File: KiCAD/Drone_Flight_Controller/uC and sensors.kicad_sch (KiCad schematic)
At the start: 7 parts, among them U401 ESP32-WROOM-32, U402 DPS368, U403 BNO055

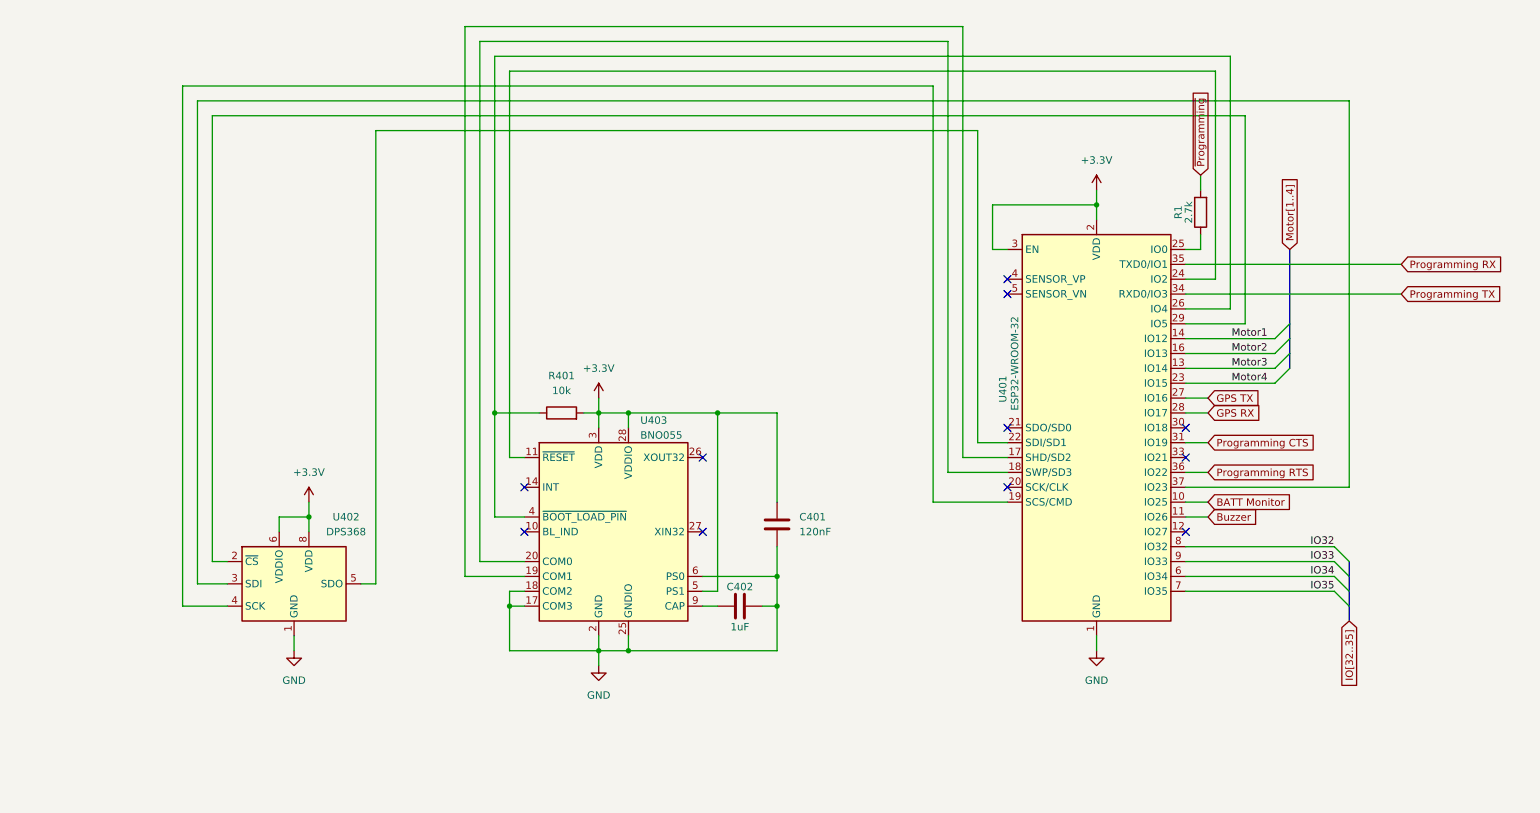
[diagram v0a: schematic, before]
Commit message: Fix SPI Connection, Disconnect wrong UART connection
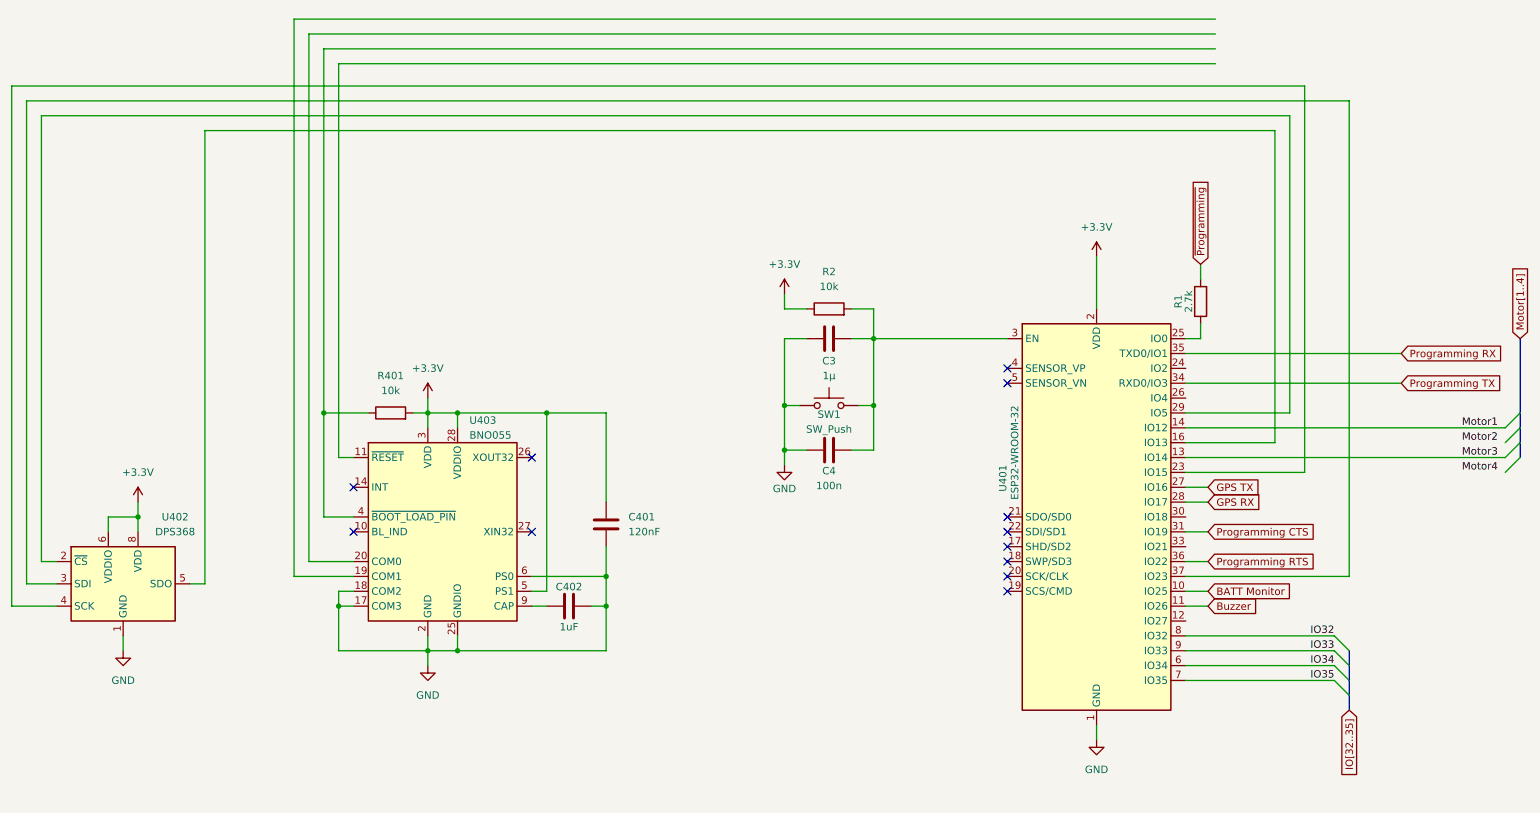
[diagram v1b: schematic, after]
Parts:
- added C3: 1µ, symbol Device:C
- added C4: 100n, Capacitor_SMD:C_0805_2012Metric_Pad1.18x1.45mm_HandSolder, symbol Device:C
- added R2: 10k, symbol Device:R
- added SW1: SW_Push, symbol Switch:SW_Push
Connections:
- net +3.3V: now also R2.1; no longer U401.3 (EN)
- net GND: now also C3.1, C4.1, SW1.1
- net Motor2: no longer U401.16 (IO13)
- net Motor4: no longer U401.23 (IO15)
- net at U401.17 (SHD/SD2): no longer U403.19 (COM1)
- net at U401.18 (SWP/SD3): no longer U403.20 (COM0)
- net at U401.19 (SCS/CMD): no longer U402.4 (SCK)
- net at U402.5 (SDO): now also U401.16 (IO13); no longer U401.22 (SDI/SD1)
- net at U401.24 (IO2): no longer U403.11 (~{RESET})
- net at R401.1, U403.4 (~{BOOT_LOAD_PIN}): no longer U401.26 (IO4)
- new net: U401.23 (IO15), U402.4 (SCK)
- new net: C3.2, C4.2, R2.2, SW1.2, U401.3 (EN)
- no-connect marks 11 -> 12
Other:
- moved on the sheet: C401, C402, R1, R401, U401, U402, U403

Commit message: Connect IMU via UART by IOMUX
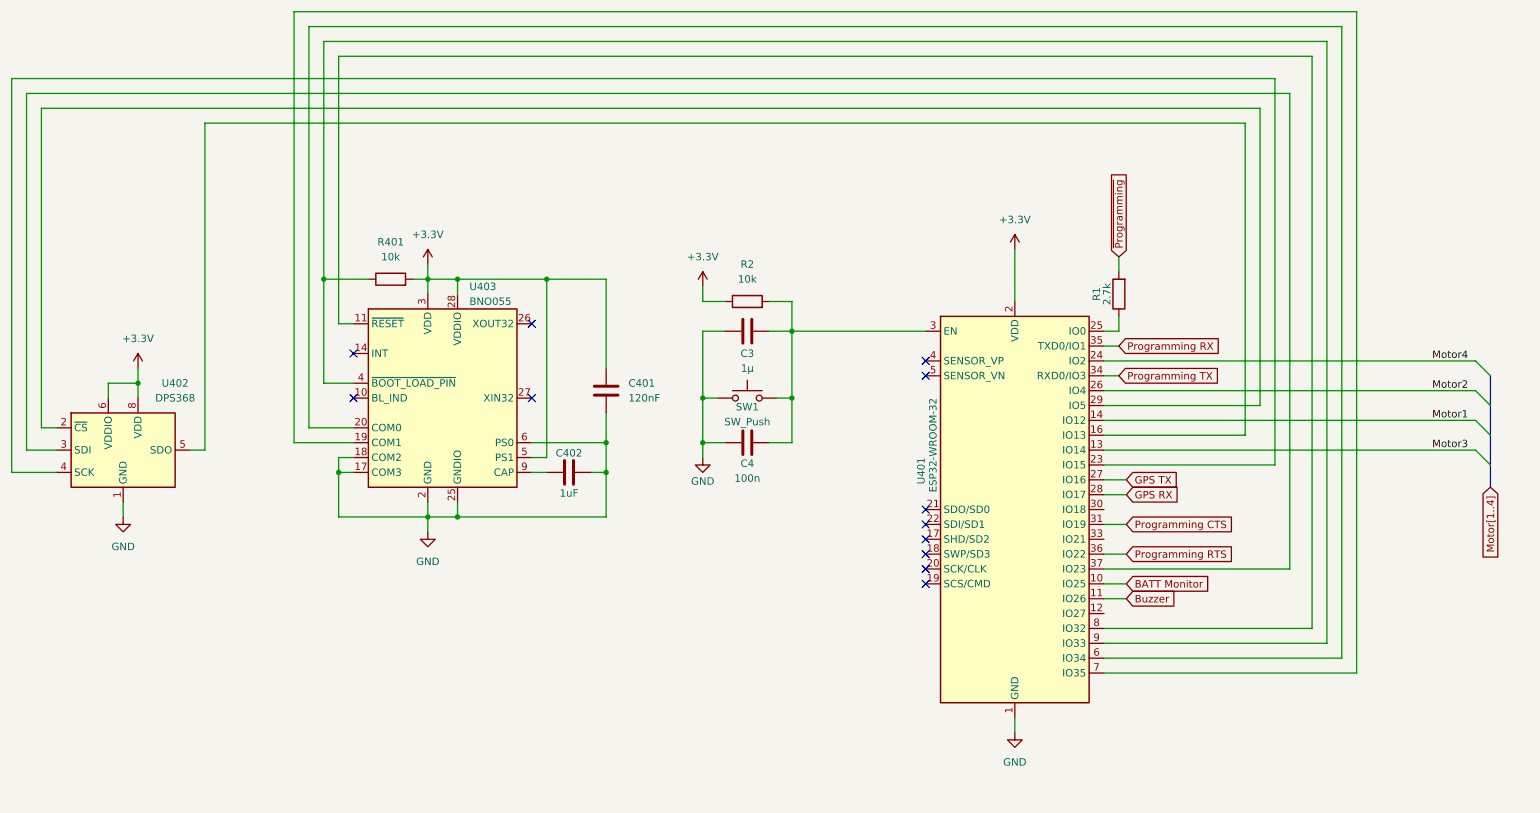
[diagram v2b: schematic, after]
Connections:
- net IO32 is gone; now on an unnamed net: U401.8 (IO32)
- net IO33 is gone; now on an unnamed net: U401.9 (IO33)
- net IO34 is gone; now on an unnamed net: U401.6 (IO34)
- net IO35 is gone; now on an unnamed net: U401.7 (IO35)
- net Motor2: now also U401.26 (IO4)
- net Motor4: now also U401.24 (IO2)
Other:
- moved on the sheet: C3, C4, C401, C402, R1, R2, R401, SW1, U401, U402, U403
